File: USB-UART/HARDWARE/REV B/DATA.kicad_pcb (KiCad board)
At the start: 2 copper layers, 18.8 x 16.3 mm, 23 parts, among them P1 USB_OTG, P2 LEFT, P3 RIGHT, U1 FT230XQ-R, U2 AP1117

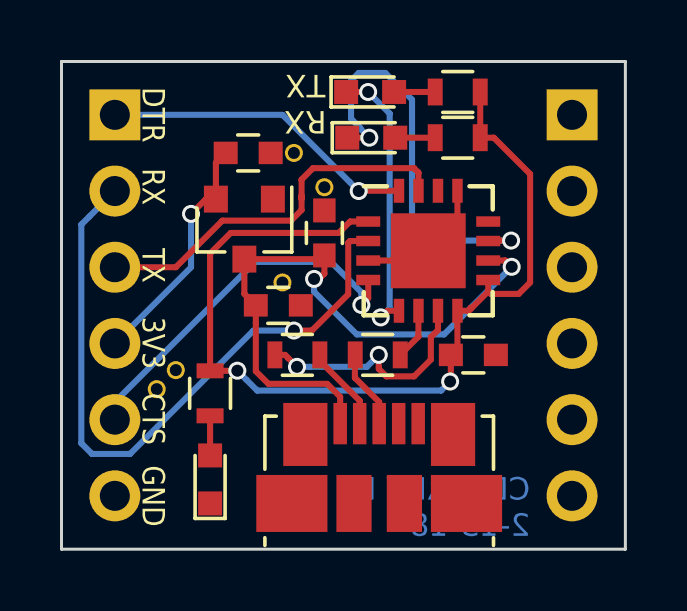
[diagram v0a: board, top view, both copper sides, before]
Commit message: Panel updates and removed AX5043
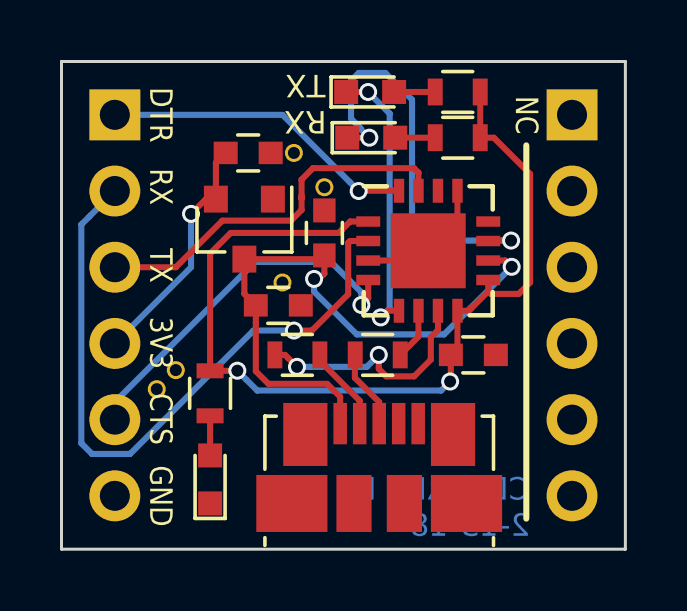
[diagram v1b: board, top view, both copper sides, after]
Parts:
- moved G*** 0.68 mm to (181.4, 107.4)
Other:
- rule pad_to_mask_clearance: 0 -> 0.05
- board text added: "NC"
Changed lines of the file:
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@@
     (links 49)
     (no_connects 0)
-    (area 175.971999 94.691999 194.868001 111.048001)
+    (area 175.822599 93.2626 195.335257 113.9014)
     (thickness 1.6)
-    (drawings 15)
+    (drawings 17)
     (tracks 154)
     (zones 0)
@@
     (pad_size 0.6 0.6)
     (pad_drill 0.4)
-    (pad_to_mask_clearance 0)
+    (pad_to_mask_clearance 0.05)
     (aux_axis_origin 0 0)
     (visible_elements FFFEFF7F)
@@
   )
   (module MOD:lightning (layer B.Cu)
-    (at 181.991 107.696)
+    (at 181.356 107.442)
     (fp_text reference G*** (at 0 0) (layer B.SilkS) hide
       (effects (font (thickness 0.3)) (justify mirror))
@@
       (xy 0.31437 1.300123) (xy 0.314354 1.28972)) (layer B.SilkS) (width 0.01))
   )
+  (gr_line (start 191.516 97.536) (end 191.516 109.982) (layer F.SilkS) (width 0.2))
+  (gr_text NC (at 191.516 95.885 270) (layer F.SilkS)
+    (effects (font (size 0.75 0.65) (thickness 0.15)) (justify left))
+  )
   (gr_text "THUNKIT\nELECTRONICS" (at 190.5 108.966) (layer B.SilkS)
     (effects (font (size 1 1) (thickness 0.15)) (justify left mirror))
@@
     (effects (font (size 1.5 1.5) (thickness 0.3)) (justify mirror))
   )
-  (gr_text GND (at 179.07 108.204 270) (layer F.SilkS)
+  (gr_text GND (at 179.324 108.204 270) (layer F.SilkS)
     (effects (font (size 0.75 0.65) (thickness 0.15)) (justify left))
   )
-  (gr_text CTS (at 179.07 105.791 270) (layer F.SilkS)
+  (gr_text CTS (at 179.324 105.791 270) (layer F.SilkS)
     (effects (font (size 0.75 0.65) (thickness 0.15)) (justify left))
   )
-  (gr_text 3V3 (at 179.07 103.251 270) (layer F.SilkS)
+  (gr_text 3V3 (at 179.324 103.251 270) (layer F.SilkS)
     (effects (font (size 0.75 0.65) (thickness 0.15)) (justify left))
   )
-  (gr_text TX (at 179.07 100.965 270) (layer F.SilkS)
+  (gr_text TX (at 179.324 100.965 270) (layer F.SilkS)
     (effects (font (size 0.75 0.65) (thickness 0.15)) (justify left))
   )
-  (gr_text RX (at 179.07 98.298 270) (layer F.SilkS)
+  (gr_text RX (at 179.324 98.298 270) (layer F.SilkS)
     (effects (font (size 0.75 0.65) (thickness 0.15)) (justify left))
   )
-  (gr_text DTR (at 179.07 96.52 270) (layer F.SilkS)
+  (gr_text DTR (at 179.324 96.52 270) (layer F.SilkS)
     (effects (font (size 0.75 0.65) (thickness 0.15)))
   )
